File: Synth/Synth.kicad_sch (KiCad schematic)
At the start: 2 parts, among them U11 LM321, U12 LM321

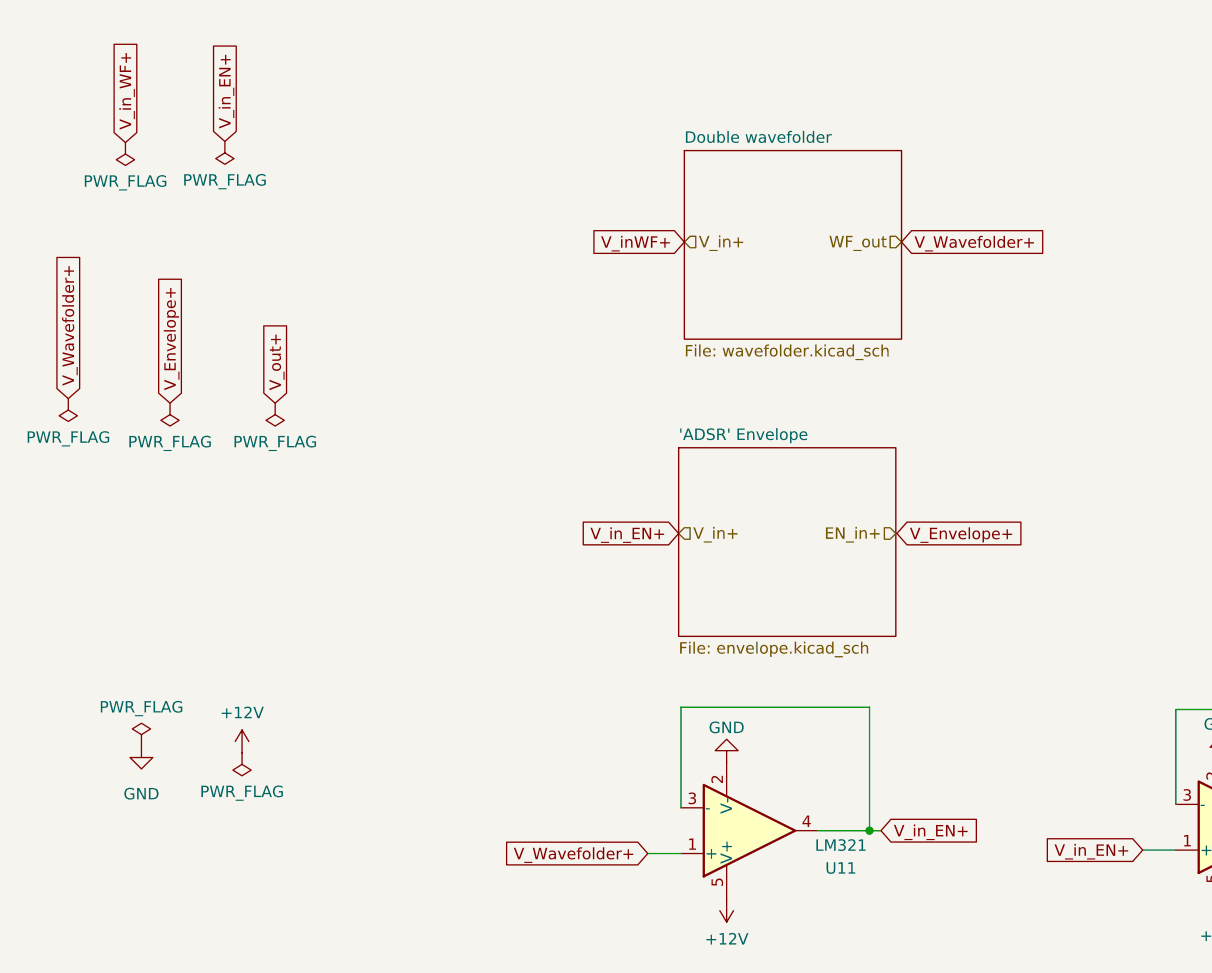
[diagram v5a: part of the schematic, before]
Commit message: fixed erc errs
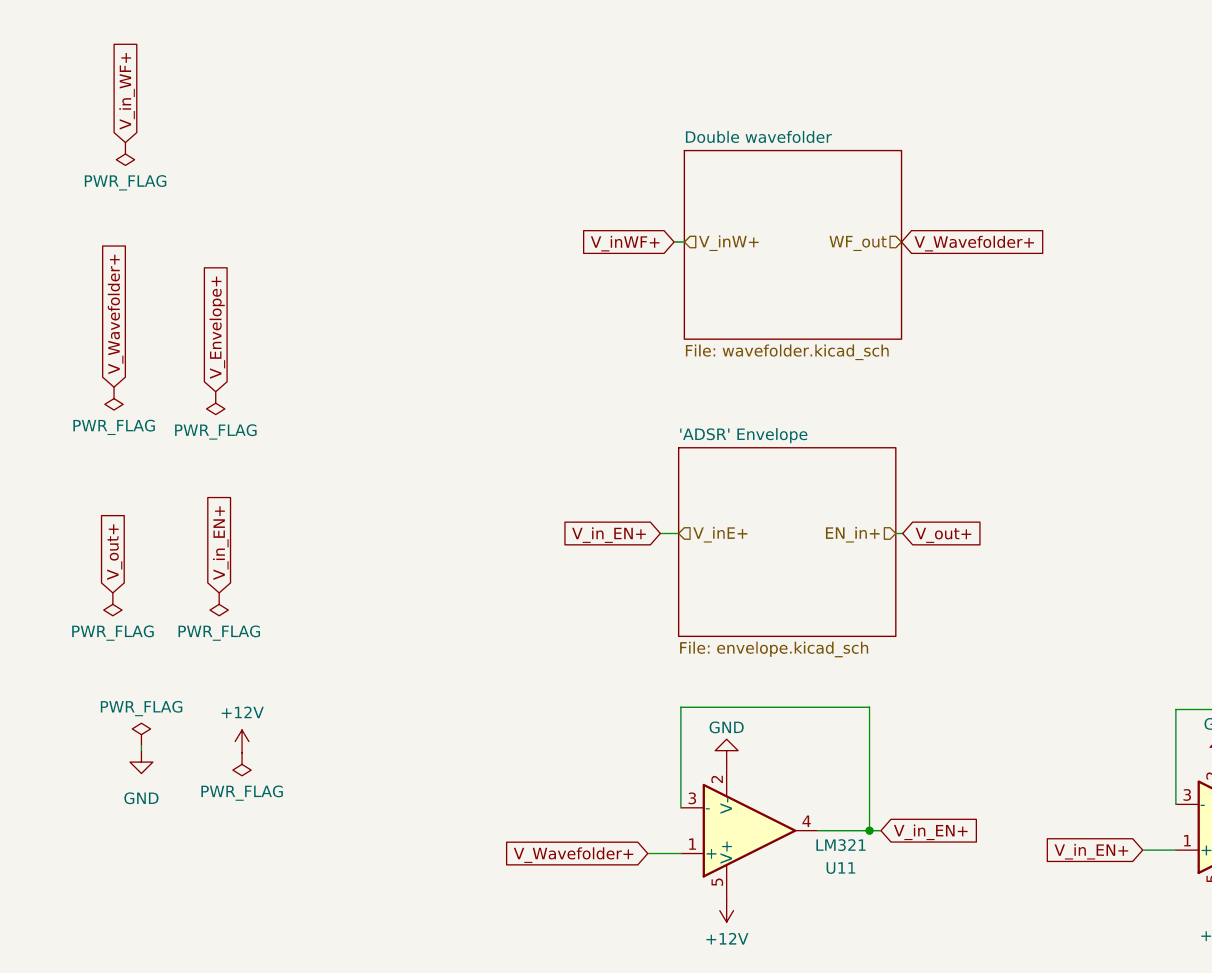
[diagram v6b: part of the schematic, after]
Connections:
- net V_inWF+: no longer U11.3 (-), U11.4, U12.1 (+)
- new net V_in_EN+: U11.3 (-), U11.4, U12.1 (+)

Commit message: add the ESP
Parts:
- added C10: 1uF, symbol Device:C
- added C7, C8, C9: 0.1uF, symbol Device:C
- added R1: 1k, symbol Device:R_Small
- added R2: 6k, symbol Device:R_Small
- added R3: 10k, symbol Device:R_Small
- added SW1: Reset, symbol Switch:SW_Push
- added SW2: Boot, symbol Switch:SW_Push
- added U1: ESP32-S2-SOLO, PCM_Espressif:ESP32-S2-SOLO, symbol PCM_Espressif:ESP32-S2-SOLO
- added U2: LM321, Package_TO_SOT_SMD:SOT-23-5, symbol Amplifier_Operational:LM321
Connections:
- net +12V: now also U2.2 (V-)
- net GND: now also C10.1, C7.1, C8.2, C9.1, R1.2, SW1.1, SW2.2, U1.1 (GND), U1.40 (GND), U1.41 (GND), U2.5 (V+)
- net V_inWF+: now also U12.3 (-), U12.4
- net V_in_EN+: no longer U12.1 (+)
- net V_out+: no longer U12.3 (-), U12.4
- new net: U1.10 (GPIO17/U1TXD/ADC2_CH6/DAC_1), U2.1 (+)
- new net: R1.1, R2.1, U2.3 (-)
- new net: C7.2, SW2.1, U1.27 (GPIO0)
- new net: C8.1, R3.2, SW1.2, U1.3 (EN)
- new net +3.3V: C10.2, C9.2, R3.1, U1.2 (3V3)
- new net ESP Out: R2.2, U2.4
- new net Filter Output: U12.1 (+)
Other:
- moved on the sheet: U11, U12

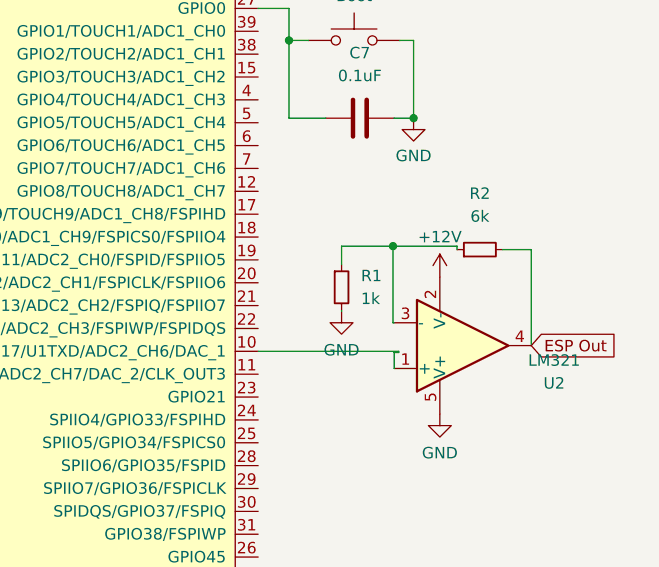
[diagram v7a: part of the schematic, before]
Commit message: changed the resistor valuess
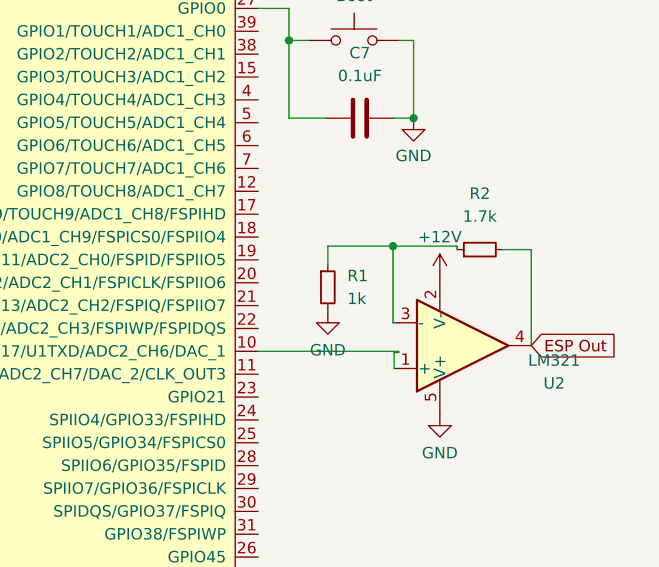
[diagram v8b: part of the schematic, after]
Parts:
- R2: value 6k -> 1.7k
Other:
- moved on the sheet: R1
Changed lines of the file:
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@@
   (junction (at 264.922 70.739) (diameter 0) (color 0 0 0 0)
   )
-  (wire (pts (xy 256.921 92.075) (xy 256.921 92.202))
+  (wire (pts (xy 255.397 92.075) (xy 255.397 92.202))
     (stroke (width 0) (type default))
   )
@@
     (stroke (width 0) (type default))
   )
-  (wire (pts (xy 256.921 86.995) (xy 256.921 84.963))
+  (wire (pts (xy 255.397 86.995) (xy 255.397 84.963))
     (stroke (width 0) (type default))
   )
@@
     (stroke (width 0) (type default))
   )
-  (wire (pts (xy 256.921 84.963) (xy 262.636 84.963))
+  (wire (pts (xy 255.397 84.963) (xy 262.636 84.963))
     (stroke (width 0) (type default))
   )
@@
       (effects (font (size 1.27 1.27)))
     )
-    (property "Value" "6k" (at 272.288 81.661 90)
+    (property "Value" "1.7k" (at 272.288 81.661 90)
       (effects (font (size 1.27 1.27)))
     )
@@
     )
   )
-  (symbol (lib_id "Device:R_Small") (at 256.921 89.535 0) (unit 1)
-    (in_bom yes) (on_board yes) (dnp no) (fields_autoplaced)
-    (property "Reference" "R1" (at 259.08 88.265 0)
+  (symbol (lib_id "Device:R_Small") (at 255.397 89.535 0) (unit 1)
+    (in_bom yes) (on_board yes) (dnp no) (fields_autoplaced)
+    (property "Reference" "R1" (at 257.556 88.265 0)
       (effects (font (size 1.27 1.27)) (justify left))
     )
-    (property "Value" "1k" (at 259.08 90.805 0)
+    (property "Value" "1k" (at 257.556 90.805 0)
       (effects (font (size 1.27 1.27)) (justify left))
     )
-    (property "Footprint" "" (at 256.921 89.535 0)
-      (effects (font (size 1.27 1.27)) hide)
-    )
-    (property "Datasheet" "~" (at 256.921 89.535 0)
+    (property "Footprint" "" (at 255.397 89.535 0)
+      (effects (font (size 1.27 1.27)) hide)
+    )
+    (property "Datasheet" "~" (at 255.397 89.535 0)
       (effects (font (size 1.27 1.27)) hide)
     )
@@
     )
   )
-  (symbol (lib_id "power:GND") (at 256.921 92.202 0) (unit 1)
-    (in_bom yes) (on_board yes) (dnp no) (fields_autoplaced)
-    (property "Reference" "#PWR038" (at 256.921 98.552 0)
-      (effects (font (size 1.27 1.27)) hide)
-    )
-    (property "Value" "GND" (at 256.921 96.52 0)
-      (effects (font (size 1.27 1.27)))
-    )
-    (property "Footprint" "" (at 256.921 92.202 0)
-      (effects (font (size 1.27 1.27)) hide)
-    )
-    (property "Datasheet" "" (at 256.921 92.202 0)
-      (effects (font (size 1.27 1.27)) hide)
-    )
+  (symbol (lib_id "power:GND") (at 255.397 92.202 0) (unit 1)
+    (in_bom yes) (on_board yes) (dnp no) (fields_autoplaced)
+    (property "Reference" "#PWR038" (at 255.397 98.552 0)
+      (effects (font (size 1.27 1.27)) hide)
+    )
+    (property "Value" "GND" (at 255.397 96.52 0)
+      (effects (font (size 1.27 1.27)))
+    )
+    (property "Footprint" "" (at 255.397 92.202 0)
+      (effects (font (size 1.27 1.27)) hide)
+    )
+    (property "Datasheet" "" (at 255.397 92.202 0)
+      (effects (font (size 1.27 1.27)) hide)
+    )
